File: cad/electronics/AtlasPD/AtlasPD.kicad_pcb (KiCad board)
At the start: 2 copper layers, 37.4 x 20 mm, 41 parts, among them J1 Conn_01x02_Male, J2 Conn_01x02_Male, J2 USB_C_Receptacle_USB2.0, SW1 SW_MEC_5E, U1 LM2678T-ADJ_NOPB, U2 ATmega328P-AU, U4 CP2104, U5 AMS1117-3.3, Y1 CSTNE16M0V53-R0

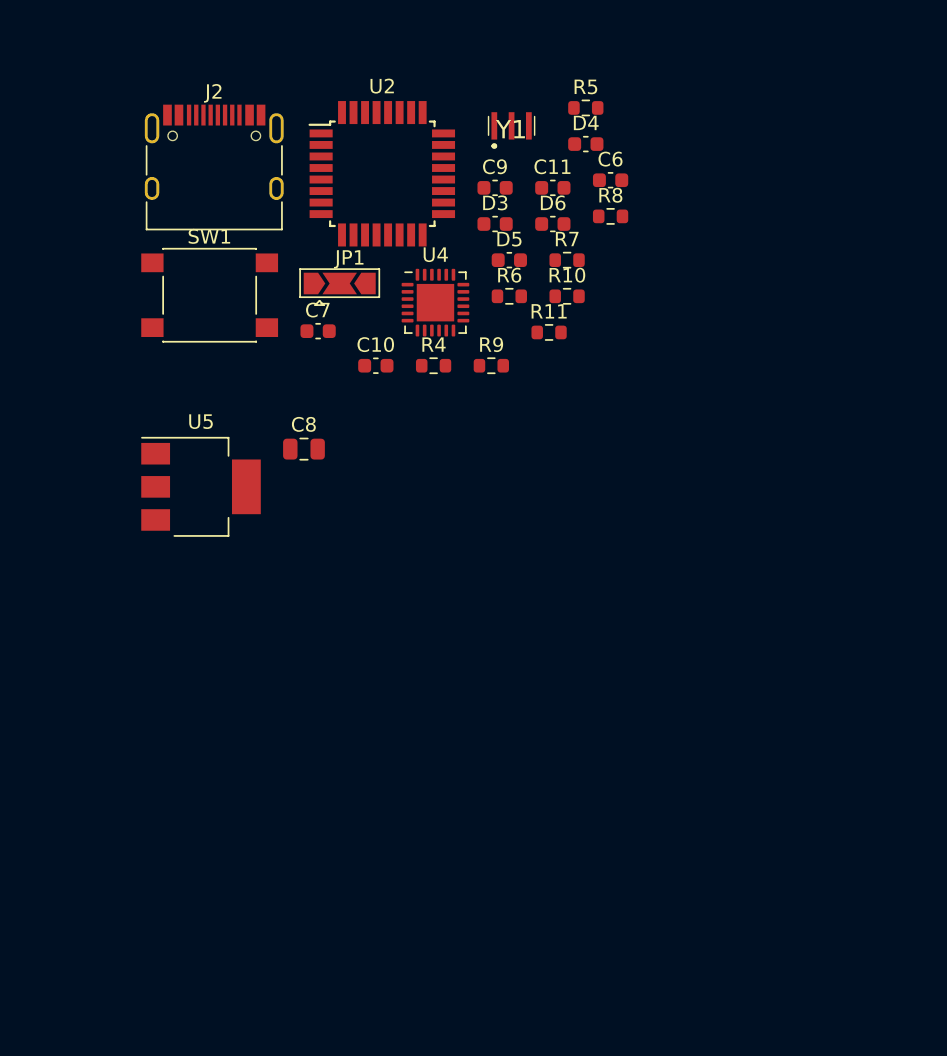
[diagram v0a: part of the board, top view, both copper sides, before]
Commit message: Started layout
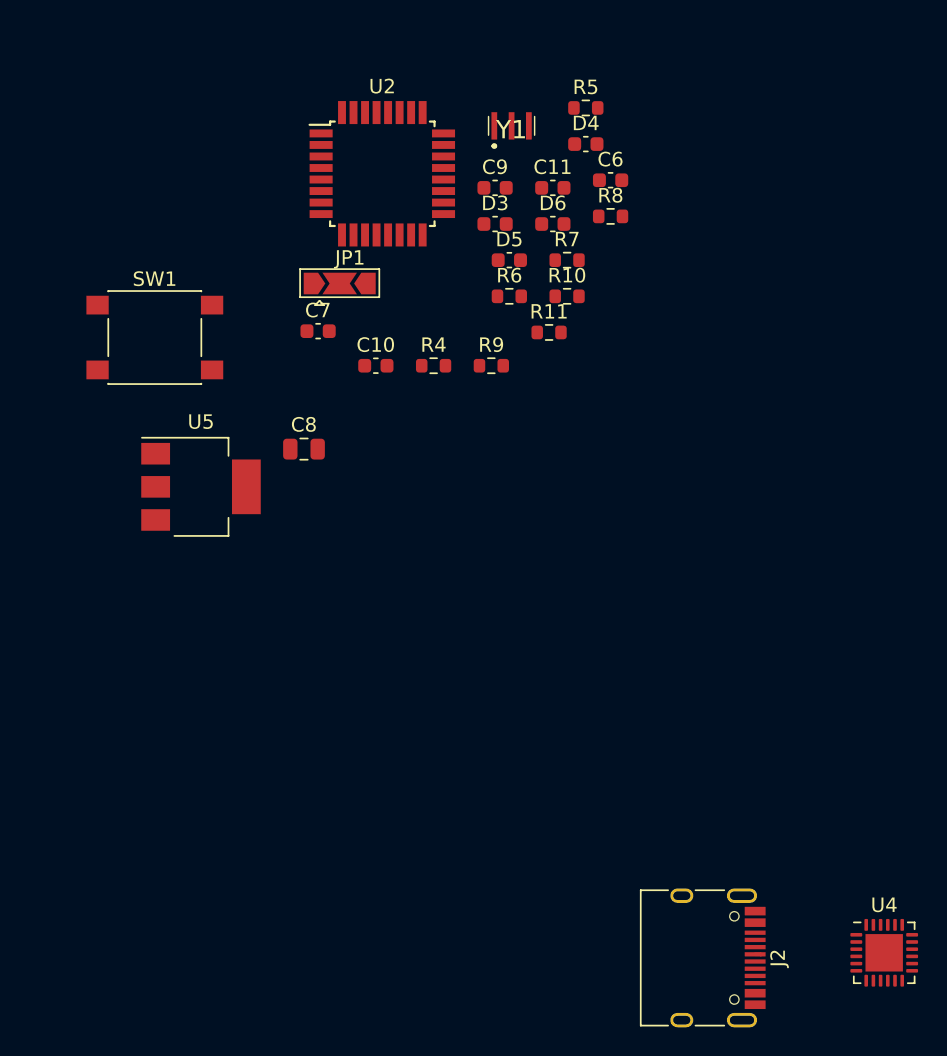
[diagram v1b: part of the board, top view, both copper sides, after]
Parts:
- SW1: value SW_MEC_5E -> SW_SPST
- moved J2 64.0 mm to (113.6, 81.5), turned to 270 degrees
- moved U4 54.9 mm to (126.6, 81.2)
- moved SW1 4.81 mm to (75.9, 38.5)
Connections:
- SW1 pad 2: Net-(C11-Pad2) -> GND
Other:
- copper layers 2 -> 4

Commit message: Forgot to save changes
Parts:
- added R12: 0, Resistor_SMD:R_0603_1608Metric, F.Cu at (120.3, 81.3)
- moved R5 58.2 mm to (135.1, 72.8)
- moved D4 56.2 mm to (140.9, 68.9), turned to 90 degrees
- moved D3 55.2 mm to (139.3, 68.9), turned to 90 degrees
- moved D5 54.6 mm to (144.3, 65.8)
- moved R7 53.2 mm to (140.9, 72.0), turned to 90 degrees
- moved R6 53.1 mm to (139.3, 72.0), turned to 90 degrees
- moved U5 49.6 mm to (122.9, 72.1), turned to 90 degrees
- moved R4 48.7 mm to (131.5, 73.0)
- moved R9 47.7 mm to (140.1, 15.7)
- moved D6 45.3 mm to (138.9, 58.9)
- moved R10 43.9 mm to (143.9, 15.9)
- moved R11 42.3 mm to (141.5, 20.0)
- moved C8 38.2 mm to (123.4, 37.1)
- moved C10 35.2 mm to (125.5, 32.1)
- moved C7 34.2 mm to (121.0, 32.2)
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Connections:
- J2 pad B7: /Sheet60A2E58A/USB_DN -> Net-(J2-PadB7)
- U4 pad 20: /Sheet60A2E58A/IO1 -> /Sheet60A2E58A/RXD
- Y1 pad 1: Net-(Y1-Pad1) -> Net-(U2-Pad8)
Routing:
- net /Sheet60A2E58A/USB_DP: track 0.41 -> 10.9 mm
- net /Sheet60A2E58A/USB_DN: track 0.00 -> 7.80 mm
- net +5V: track 0.00 -> 7.62 mm
- net Net-(J2-PadB7): track 0.00 -> 2.85 mm
- added copper zone on F.Cu, net +3V3

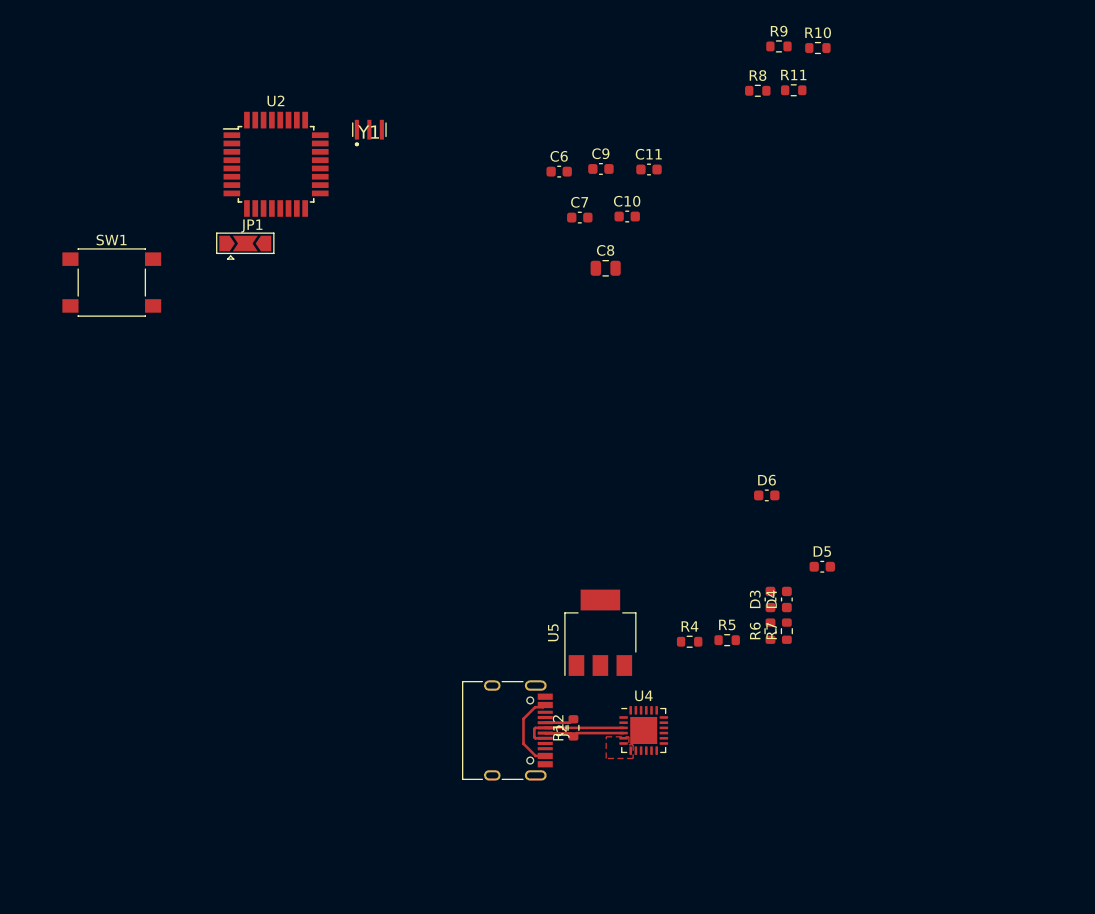
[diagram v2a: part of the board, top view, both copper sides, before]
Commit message: Layout updates, new PMICs for motors
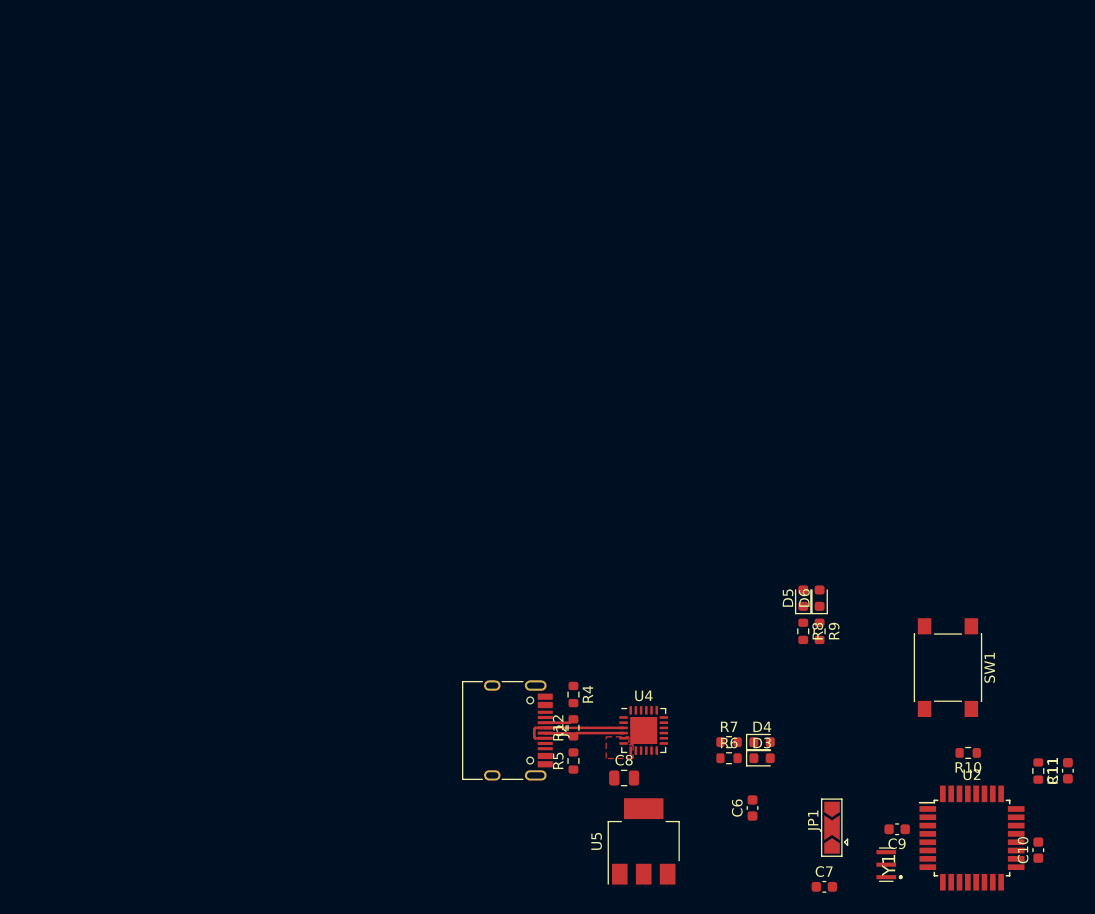
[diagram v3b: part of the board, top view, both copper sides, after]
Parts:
- D3, D4, D5, D6: footprint Capacitor_SMD:C_0603_1608Metric -> LED_SMD:LED_0603_1608Metric
- moved U2 93.2 mm to (158.7, 91.9)
- moved SW1 88.5 mm to (156.4, 75.5), turned to 270 degrees
- moved Y1 86.3 mm to (150.9, 94.4), turned to 90 degrees
- moved JP1 79.6 mm to (145.2, 90.9), turned to 90 degrees
- moved C10 72.6 mm to (165.0, 93.0), turned to 90 degrees
- moved C11 70.5 mm to (167.9, 85.4), turned to 90 degrees
- moved C9 69.6 mm to (151.5, 91.0), turned to 180 degrees
- moved R11 69.6 mm to (165.0, 85.4), turned to 270 degrees
- moved R10 69.3 mm to (158.3, 83.7), turned to 180 degrees
- moved C7 68.5 mm to (144.5, 96.6)
- moved C6 64.0 mm to (137.6, 89.0), turned to 90 degrees
- moved R9 56.4 mm to (144.0, 72.0), turned to 270 degrees
- moved R8 52.2 mm to (142.4, 72.0), turned to 270 degrees
- moved C8 49.1 mm to (125.2, 86.1)
- moved U5 20.5 mm to (127.1, 92.2)
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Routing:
- net +5V: track 7.62 -> 0.00 mm

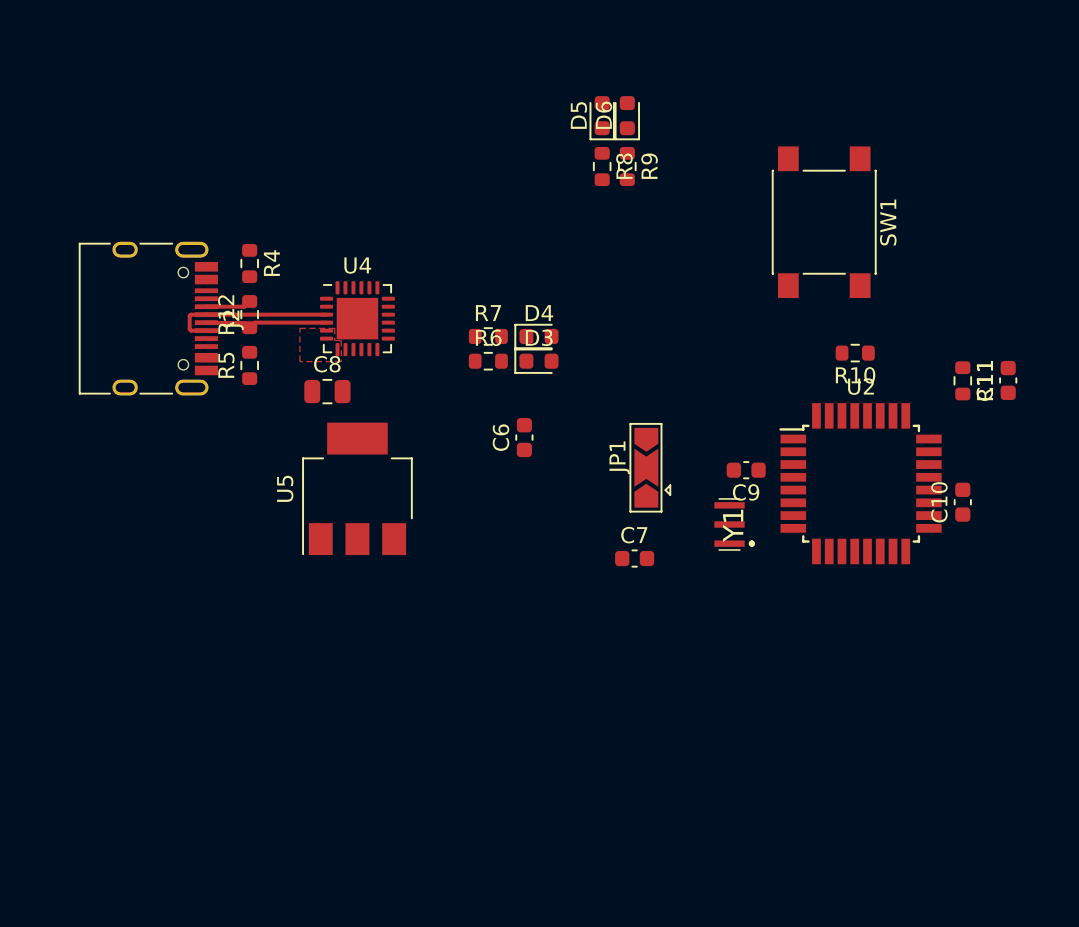
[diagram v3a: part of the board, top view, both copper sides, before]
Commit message: Added logic gates
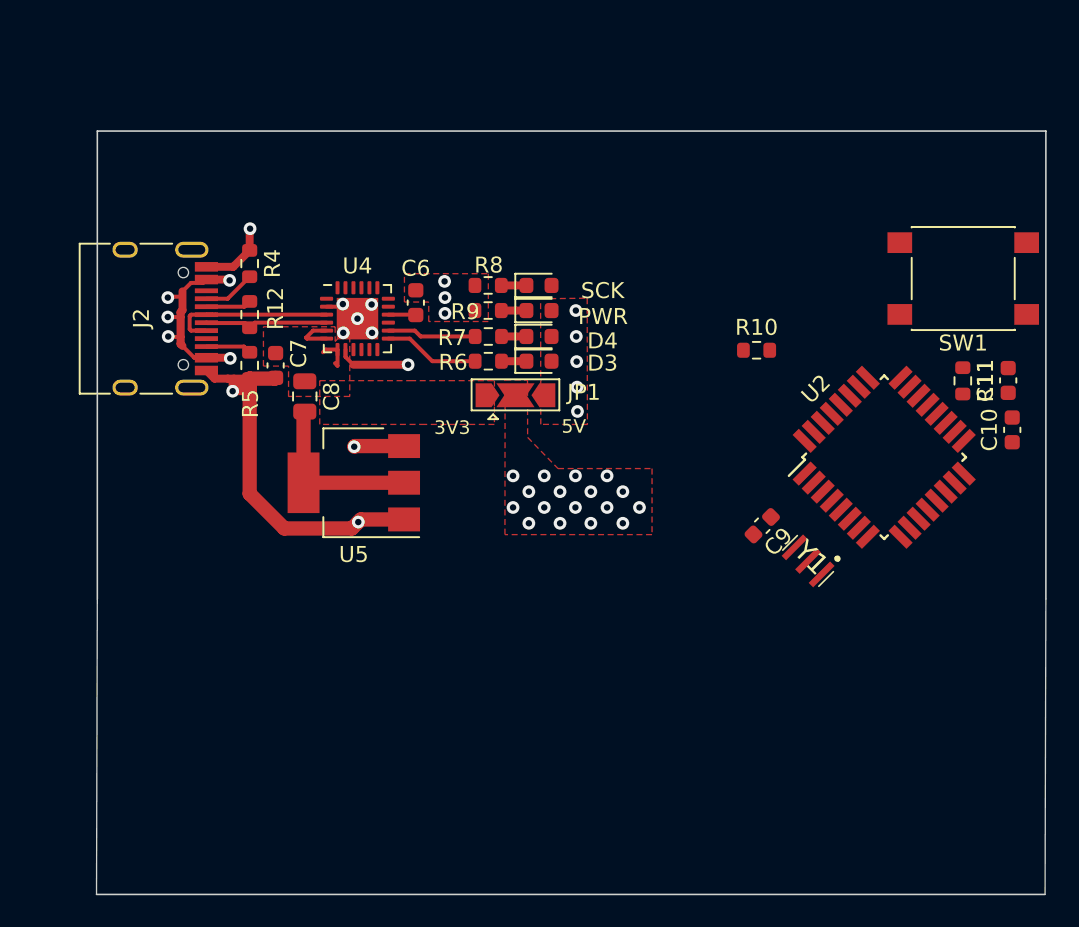
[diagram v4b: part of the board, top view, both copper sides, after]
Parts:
- moved C7 25.6 mm to (122.0, 84.5), turned to 90 degrees
- moved PWR 13.4 mm to (138.5, 81.0), turned to 0 degrees
- moved R9 12.6 mm to (135.3, 81.0), turned to 180 degrees
- moved SCK 11.4 mm to (138.5, 79.5), turned to 0 degrees
- moved C6 10.9 mm to (130.8, 80.5), turned to 270 degrees
- moved R8 10.3 mm to (135.3, 79.5), turned to 180 degrees
- moved SW1 9.40 mm to (165.1, 79.0), turned to 180 degrees
- moved JP1 9.38 mm to (137.0, 86.3), turned to 0 degrees
- moved R10 6.19 mm to (152.1, 83.5), turned to 0 degrees
- moved C10 5.49 mm to (168.1, 88.5)
- moved Y1 5.19 mm to (155.7, 96.4), turned to 135 degrees
- moved C9 3.62 mm to (152.5, 94.5), turned to 225 degrees
- moved U2 2.20 mm to (160.1, 90.2), turned to 45 degrees
- moved C8 1.45 mm to (123.8, 86.4), turned to 270 degrees
- moved U5 0.44 mm to (126.9, 91.8), turned to 180 degrees
- renumbered D6 to PWR, D5 to SCK
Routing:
- net GND: track 2.56 -> 34.8 mm, vias 34 -> 45
- net +5V: track 0.00 -> 24.0 mm, vias 0 -> 12
- net Net-(C8-Pad2): track 0.00 -> 10.8 mm
- net Net-(R6-Pad1): track 0.00 -> 6.03 mm
- net Net-(R7-Pad1): track 0.00 -> 5.59 mm
- net +3V3: track 0.00 -> 5.02 mm
- net Net-(J2-PadA5): track 0.00 -> 3.28 mm
- net Net-(J2-PadB5): track 0.00 -> 2.86 mm
- net Net-(C6-Pad2): track 0.00 -> 1.73 mm
- net Net-(D5-Pad1): track 0.00 -> 1.58 mm
- net Net-(D6-Pad1): track 0.00 -> 1.57 mm
- net Net-(D4-Pad1): track 0.00 -> 1.56 mm
- net Net-(D3-Pad1): track 0.00 -> 1.56 mm
- net VCC: vias 0 -> 17
- added copper zone on F.Cu, net +5V
- added copper zone on In2.Cu, net +5V
- added copper zone on In1.Cu, net GND
- added copper zone on F.Cu, net VCC
- added copper zone on In2.Cu, net VCC
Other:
- board size 37.4 x 20 mm -> 148.2 x 100.5 mm
- board text added: "3V3"
- board text added: "5V"

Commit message: Project Restructuring for ease of design and other stuff
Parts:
- added BT1: Battery_Cell, Battery:BatteryHolder_Keystone_1042_1x18650, F.Cu at (60.0, 137.6)
- added BT2: Battery_Cell, Battery:BatteryHolder_Keystone_1042_1x18650, F.Cu at (60.0, 114.9)
- added J3: Conn_01x06, Connector_JST:JST_PH_B6B-PH-K_1x06_P2.00mm_Vertical, F.Cu at (166.5, 113.4)
- added J4: Conn_01x06, Connector_JST:JST_PH_B6B-PH-K_1x06_P2.00mm_Vertical, F.Cu at (157.5, 103.7)
- added U3: 74LS08, Package_SO:SOIC-14_3.9x8.7mm_P1.27mm, F.Cu at (145.4, 105.3)
- added U6: DRV8837C, Package_SON:WSON-8-1EP_2x2mm_P0.5mm_EP0.9x1.6mm, F.Cu at (152.2, 103.4)
- added U7: DRV8837C, Package_SON:WSON-8-1EP_2x2mm_P0.5mm_EP0.9x1.6mm, F.Cu at (162.4, 113.3)
- renumbered SCK to D5, PWR to D6
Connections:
- C1 pad 1: Net-(C1-Pad1) -> +BATT
- C2 pad 1: Net-(C1-Pad1) -> +BATT
- U1 pad 2: Net-(C1-Pad1) -> +BATT

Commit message: Found a bug, squashed it
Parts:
- added J1: Barrel_Jack_MountingPin, Connector_BarrelJack:BarrelJack_Horizontal, F.Cu at (124.6, 104.6)
- added REF**: KiCad-Logo2_5mm_SilkScreen, Symbol:KiCad-Logo2_5mm_SilkScreen, F.Cu at (128.0, 73.5)
- C8: footprint Capacitor_SMD:C_0805_2012Metric -> Capacitor_SMD:C_0603_1608Metric
- moved J4 19.9 mm to (140.9, 114.8), turned to 180 degrees
- moved C11 11.7 mm to (156.2, 84.5), turned to 270 degrees
- moved J3 10.4 mm to (156.2, 114.8), turned to 180 degrees
- moved U5 6.54 mm to (120.3, 91.4), turned to 0 degrees
- moved C10 3.43 mm to (166.7, 85.4)
- moved R10 3.22 mm to (154.7, 85.5), turned to 270 degrees
- moved C9 2.37 mm to (154.8, 94.8)
- moved Y1 1.80 mm to (157.4, 96.6)
- moved C8 1.38 mm to (122.5, 86.8), turned to 180 degrees
- moved U3 1.08 mm to (145.1, 104.3)
- moved U7 0.69 mm to (162.4, 112.6), turned to 180 degrees
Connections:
- net /Sheet60A2E58A/IO13_SCK renamed /Sheet60A2E58A/EN_MTRS
- C8 pad 2: Net-(C8-Pad2) -> GND
- U3 pad 14: +5V -> VCC
- U4 pad 20: /Sheet60A2E58A/RXD -> /Sheet60A2E58A/IO1
- U4 pad 21: /Sheet60A2E58A/IO1 -> /Sheet60A2E58A/RXD
- U5 pad 2: Net-(C8-Pad2) -> +3V3
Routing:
- net VCC: track 0.00 -> 54.2 mm, vias 17 -> 20
- net /Motor Driver/PWM_A: track 0.00 -> 36.4 mm, vias 0 -> 2
- net /Sheet60A2E58A/DTR: track 0.00 -> 34.5 mm
- net /Sheet60A2E58A/IO1: track 0.00 -> 32.8 mm
- net /Sheet60A2E58A/RXD: track 0.00 -> 31.6 mm
- net /Sheet60A2E58A/EN_MTRS: track 0.00 -> 31.3 mm, vias 0 -> 2
- net /Motor Driver/IN2: track 0.00 -> 30.4 mm
- net /Motor Driver/PWM_B: track 0.00 -> 29.2 mm, vias 0 -> 2
- net /Motor Driver/IN1: track 0.00 -> 27.5 mm
- net /Motor Driver/IN4: track 0.00 -> 24.9 mm, vias 0 -> 2
- net +5V: track 24.0 -> 45.2 mm, vias 12 -> 19
- net Net-(C11-Pad2): track 0.00 -> 20.3 mm
- net /Motor Driver/IN3: track 0.00 -> 17.1 mm
- net GND: track 34.8 -> 20.8 mm, vias 45 -> 46
- net Net-(C8-Pad2): track 10.8 -> 0.00 mm
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
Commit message: Power board layout
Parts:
- moved REF** 139.0 mm to (127.6, 140.2), turned to 180 degrees
- moved J2 133.8 mm to (126.9, 110.3), turned to 270 degrees
- moved C1 133.6 mm to (124.8, 135.4), turned to 180 degrees
- moved D1 132.8 mm to (126.3, 118.9), turned to 90 degrees
- moved C4 132.5 mm to (126.1, 113.4), turned to 0 degrees
- moved J1 129.7 mm to (120.8, 140.5), turned to 270 degrees
- moved U1 128.4 mm to (122.3, 129.0), turned to 180 degrees
- moved L1 128.0 mm to (123.0, 117.2), turned to 90 degrees
- moved C3 128.0 mm to (122.8, 121.1), turned to 180 degrees
- moved C2 126.3 mm to (119.3, 136.7), turned to 90 degrees
- moved C5 124.9 mm to (120.7, 112.2), turned to 180 degrees
- moved R1 123.4 mm to (119.7, 118.1), turned to 270 degrees
- moved R2 122.6 mm to (119.0, 121.1), turned to 180 degrees
- moved R3 118.1 mm to (115.8, 119.4), turned to 270 degrees
- moved D2 117.9 mm to (115.8, 115.6), turned to 90 degrees
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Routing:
- net Net-(BT1-Pad2): track 0.00 -> 22.7 mm
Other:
- board size 148.2 x 100.5 mm -> 150.2 x 117.8 mm
